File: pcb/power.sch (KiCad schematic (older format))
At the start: 27 parts, among them J2 BARREL_JACK, Q1 MMBTA92, Q2 STD5N52U, U10 MC34063A, U9 MC34063A

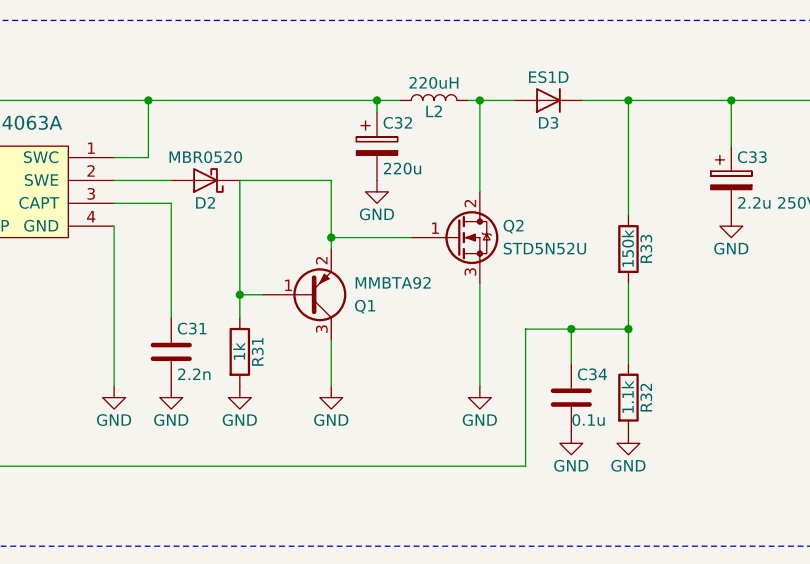
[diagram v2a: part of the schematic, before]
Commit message: Switched to nodemcu-style flashing circuitry.
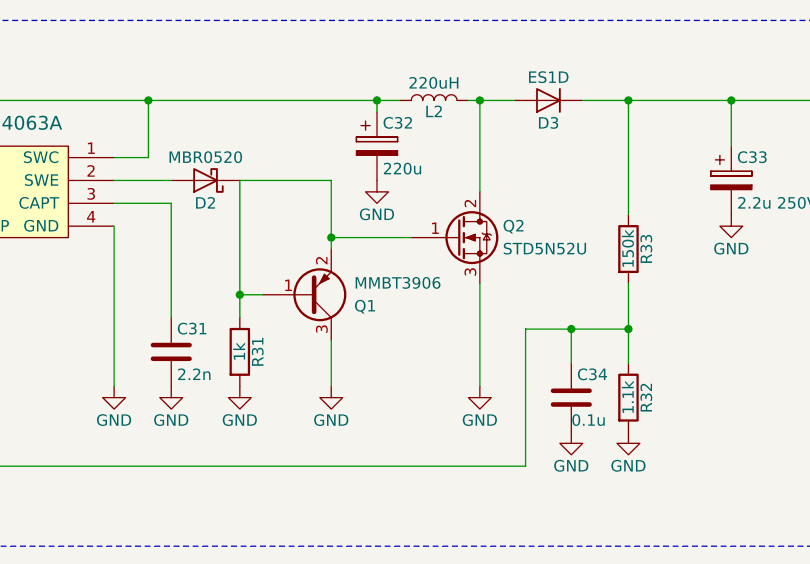
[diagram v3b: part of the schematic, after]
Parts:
- Q1: value MMBTA92 -> MMBT3906
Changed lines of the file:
@@
 Sheet 3 4
 Title "Eighty-Two Nixie-Six: Internet Radio Alarm Clock"
-Date "2017-04-18"
+Date "2017-04-20"
 Rev "1.1"
 Comp ""
 Comment1 "Licensed under MPL 2.0"
-Comment2 ""
-Comment3 ""
+Comment2 "https://git.io/v9fmR"
+Comment3 "By Austin R. Leydecker"
 Comment4 ""
 $EndDescr
@@
 $EndComp
 $Comp
-L GND #PWR068
+L GND #PWR063
 U 1 1 58CA2194
 P 4450 3400
-F 0 "#PWR068" H 4450 3150 50  0001 C CNN
+F 0 "#PWR063" H 4450 3150 50  0001 C CNN
 F 1 "GND" H 4450 3250 50  0000 C CNN
 F 2 "" H 4450 3400 50  0000 C CNN
@@
 $EndComp
 $Comp
-L GND #PWR069
+L GND #PWR064
 U 1 1 58CA327D
 P 2050 3400
-F 0 "#PWR069" H 2050 3150 50  0001 C CNN
+F 0 "#PWR064" H 2050 3150 50  0001 C CNN
 F 1 "GND" H 2050 3250 50  0000 C CNN
 F 2 "" H 2050 3400 50  0000 C CNN
@@
 $EndComp
 $Comp
-L GND #PWR070
+L GND #PWR065
 U 1 1 58CA32A3
 P 2300 3400
-F 0 "#PWR070" H 2300 3150 50  0001 C CNN
+F 0 "#PWR065" H 2300 3150 50  0001 C CNN
 F 1 "GND" H 2300 3250 50  0000 C CNN
 F 2 "" H 2300 3400 50  0000 C CNN
@@
 $EndComp
 $Comp
-L GND #PWR071
+L GND #PWR066
 U 1 1 58CA32C9
 P 2500 3400
-F 0 "#PWR071" H 2500 3150 50  0001 C CNN
+F 0 "#PWR066" H 2500 3150 50  0001 C CNN
 F 1 "GND" H 2500 3250 50  0000 C CNN
 F 2 "" H 2500 3400 50  0000 C CNN
@@
 $EndComp
 $Comp
-L GND #PWR072
+L GND #PWR067
 U 1 1 58CA36A9
 P 1550 4050
-F 0 "#PWR072" H 1550 3800 50  0001 C CNN
+F 0 "#PWR067" H 1550 3800 50  0001 C CNN
 F 1 "GND" H 1550 3900 50  0000 C CNN
 F 2 "" H 1550 4050 50  0000 C CNN
@@
 $EndComp
 $Comp
-L GND #PWR073
+L GND #PWR068
 U 1 1 58CA3899
 P 3550 4050
-F 0 "#PWR073" H 3550 3800 50  0001 C CNN
+F 0 "#PWR068" H 3550 3800 50  0001 C CNN
 F 1 "GND" H 3550 3900 50  0000 C CNN
 F 2 "" H 3550 4050 50  0000 C CNN
@@
 $EndComp
 $Comp
-L GND #PWR074
+L GND #PWR069
 U 1 1 58CA5F0C
 P 8550 2900
-F 0 "#PWR074" H 8550 2650 50  0001 C CNN
+F 0 "#PWR069" H 8550 2650 50  0001 C CNN
 F 1 "GND" H 8550 2750 50  0000 C CNN
 F 2 "" H 8550 2900 50  0000 C CNN
@@
 $EndComp
 $Comp
-L GND #PWR075
+L GND #PWR070
 U 1 1 58CA6586
 P 7650 3800
-F 0 "#PWR075" H 7650 3550 50  0001 C CNN
+F 0 "#PWR070" H 7650 3550 50  0001 C CNN
 F 1 "GND" H 7650 3650 50  0000 C CNN
 F 2 "" H 7650 3800 50  0000 C CNN
@@
 $EndComp
 $Comp
-L GND #PWR076
+L GND #PWR071
 U 1 1 58CA65BC
 P 7400 3800
-F 0 "#PWR076" H 7400 3550 50  0001 C CNN
+F 0 "#PWR071" H 7400 3550 50  0001 C CNN
 F 1 "GND" H 7400 3650 50  0000 C CNN
 F 2 "" H 7400 3800 50  0000 C CNN
@@
 P 8250 3400
 F 0 "Q1" H 8450 3450 50  0000 L CNN
-F 1 "MMBTA92" H 8450 3350 50  0000 L CNN
+F 1 "MMBT3906" H 8450 3350 50  0000 L CNN
 F 2 "TO_SOT_Packages_SMD:SOT-23_Handsoldering" H 8450 3500 50  0001 C CNN
 F 3 "" H 8250 3400 50  0000 C CNN
@@
 Connection ~ 7950 3400
 $Comp
-L GND #PWR077
+L GND #PWR072
 U 1 1 58CA8184
 P 7950 3800
-F 0 "#PWR077" H 7950 3550 50  0001 C CNN
+F 0 "#PWR072" H 7950 3550 50  0001 C CNN
 F 1 "GND" H 7950 3650 50  0000 C CNN
 F 2 "" H 7950 3800 50  0000 C CNN
@@
 $EndComp
 $Comp
-L GND #PWR078
+L GND #PWR073
 U 1 1 58CA8203
 P 8350 3800
-F 0 "#PWR078" H 8350 3550 50  0001 C CNN
+F 0 "#PWR073" H 8350 3550 50  0001 C CNN
 F 1 "GND" H 8350 3650 50  0000 C CNN
 F 2 "" H 8350 3800 50  0000 C CNN
@@
 $EndComp
 $Comp
-L GND #PWR079
+L GND #PWR074
 U 1 1 58CA95C3
 P 5500 3400
-F 0 "#PWR079" H 5500 3150 50  0001 C CNN
+F 0 "#PWR074" H 5500 3150 50  0001 C CNN
 F 1 "GND" H 5500 3250 50  0000 C CNN
 F 2 "" H 5500 3400 50  0000 C CNN
@@
 $EndComp
 $Comp
-L GND #PWR080
+L GND #PWR075
 U 1 1 58CAFEE9
 P 9000 3800
-F 0 "#PWR080" H 9000 3550 50  0001 C CNN
+F 0 "#PWR075" H 9000 3550 50  0001 C CNN
 F 1 "GND" H 9000 3650 50  0000 C CNN
 F 2 "" H 9000 3800 50  0000 C CNN
@@
 Connection ~ 10100 2550
 $Comp
-L GND #PWR081
+L GND #PWR076
 U 1 1 58CB3A22
 P 10100 3050
-F 0 "#PWR081" H 10100 2800 50  0001 C CNN
+F 0 "#PWR076" H 10100 2800 50  0001 C CNN
 F 1 "GND" H 10100 2900 50  0000 C CNN
 F 2 "" H 10100 3050 50  0000 C CNN
@@
 $EndComp
 $Comp
-L GND #PWR082
+L GND #PWR077
 U 1 1 58CB5066
 P 9650 4000
-F 0 "#PWR082" H 9650 3750 50  0001 C CNN
+F 0 "#PWR077" H 9650 3750 50  0001 C CNN
 F 1 "GND" H 9650 3850 50  0000 C CNN
 F 2 "" H 9650 4000 50  0000 C CNN
@@
 	5000 1800 4700 1800
 $Comp
-L GND #PWR083
+L GND #PWR078
 U 1 1 58CEA1F0
 P 4800 2100
-F 0 "#PWR083" H 4800 1850 50  0001 C CNN
+F 0 "#PWR078" H 4800 1850 50  0001 C CNN
 F 1 "GND" H 4800 1950 50  0000 C CNN
 F 2 "" H 4800 2100 50  0000 C CNN
@@
 $EndComp
 $Comp
-L GND #PWR084
+L GND #PWR079
 U 1 1 58E03055
 P 9400 4000
-F 0 "#PWR084" H 9400 3750 50  0001 C CNN
+F 0 "#PWR079" H 9400 3750 50  0001 C CNN
 F 1 "GND" H 9400 3850 50  0000 C CNN
 F 2 "" H 9400 4000 50  0000 C CNN

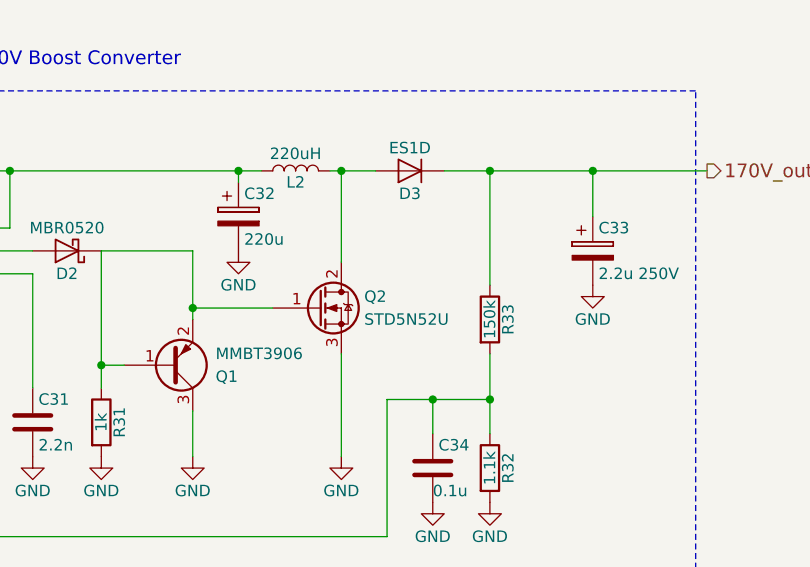
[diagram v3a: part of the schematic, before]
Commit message: Swapped Q2 for cheaper STN1NK60Z. Fixed some ground plane issues.
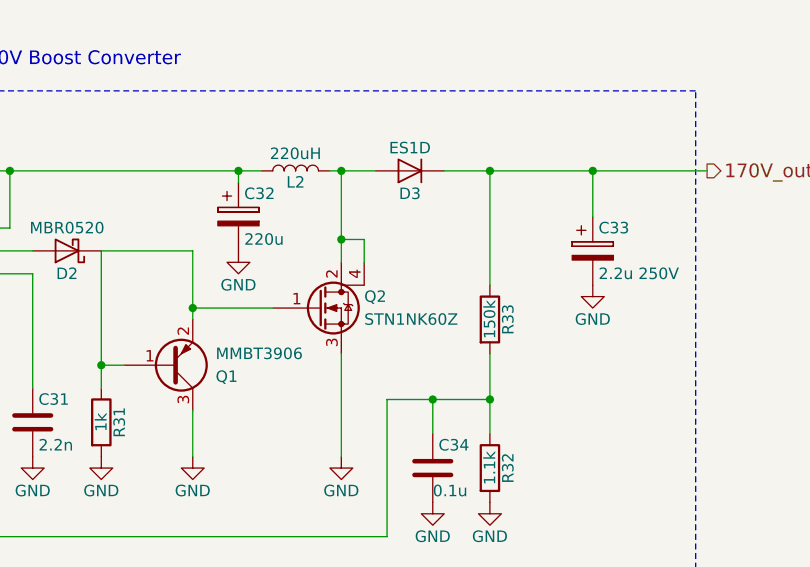
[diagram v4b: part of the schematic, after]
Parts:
- removed Q2: STD5N52U, TO_SOT_Packages_SMD:TO-252-2Lead, symbol Q_NMOS_GDS
- added Q2: STN1NK60Z, TO_SOT_Packages_SMD:SOT-223, symbol Q_NMOS_GDSD
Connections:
- net GND: now also Q2.3 (S)
- net at D2.1 (K), Q1.1 (B), Q1.2 (E)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: now also Q2.1 (G)
- net at D3.2 (A), L2.1: now also Q2.2 (D), Q2.4 (D)
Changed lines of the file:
@@
-$EndComp
-$Comp
-L Q_NMOS_GDS Q2
-U 1 1 58CA9BC8
-P 8900 3150
-F 0 "Q2" H 9100 3200 50  0000 L CNN
-F 1 "STD5N52U" H 9100 3100 50  0000 L CNN
-F 2 "TO_SOT_Packages_SMD:TO-252-2Lead" H 9100 3250 50  0001 C CNN
-F 3 "" H 8900 3150 50  0000 C CNN
-	1    8900 3150
-	1    0    0    -1
 $EndComp
 $Comp
@@
 	9200 3550 9200 4150
 Connection ~ 9400 3550
+$Comp
+L Q_NMOS_GDSD Q2
+U 1 1 58FA9AB6
+P 8900 3150
+F 0 "Q2" H 9100 3200 50  0000 L CNN
+F 1 "STN1NK60Z" H 9100 3100 50  0000 L CNN
+F 2 "TO_SOT_Packages_SMD:SOT-223" H 9100 3250 50  0001 C CNN
+F 3 "" H 8900 3150 50  0000 C CNN
+	1    8900 3150
+	1    0    0    -1
+$EndComp
+Wire Wire Line
+	9000 2850 9100 2850
+Wire Wire Line
+	9100 2850 9100 2950
+Connection ~ 9000 2850
 $EndSCHEMATC
